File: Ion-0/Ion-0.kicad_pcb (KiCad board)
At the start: 4 copper layers, 54.6 x 86.4 mm, 96 parts, among them J1 Beaglebone-green-P9, J10 Conn_CAN, J11 Conn_Prob_1, J12 Conn_Prob_2, J13 Conn_01x04, J2 Beaglebone-green-P8, J3 Conn_02x06_Odd_Even, J4 Conn_02x06_Odd_Even, J5 Conn_02x06_Odd_Even, J6 Coaxial_Small, J8 Conn_Heater, J9 Conn_prob_3, Q1 IRLML6244, Q2 IRLML6244, U1 HDC2080, U2 MS5607-02BA, U3 BNO085, U4 TCA9617ADGKR, U6 MAX-M10M-00B, U7 TPS3850H50DRCR, U8 SN65HVD230, Y2 9HT10-32.768KBZF-T

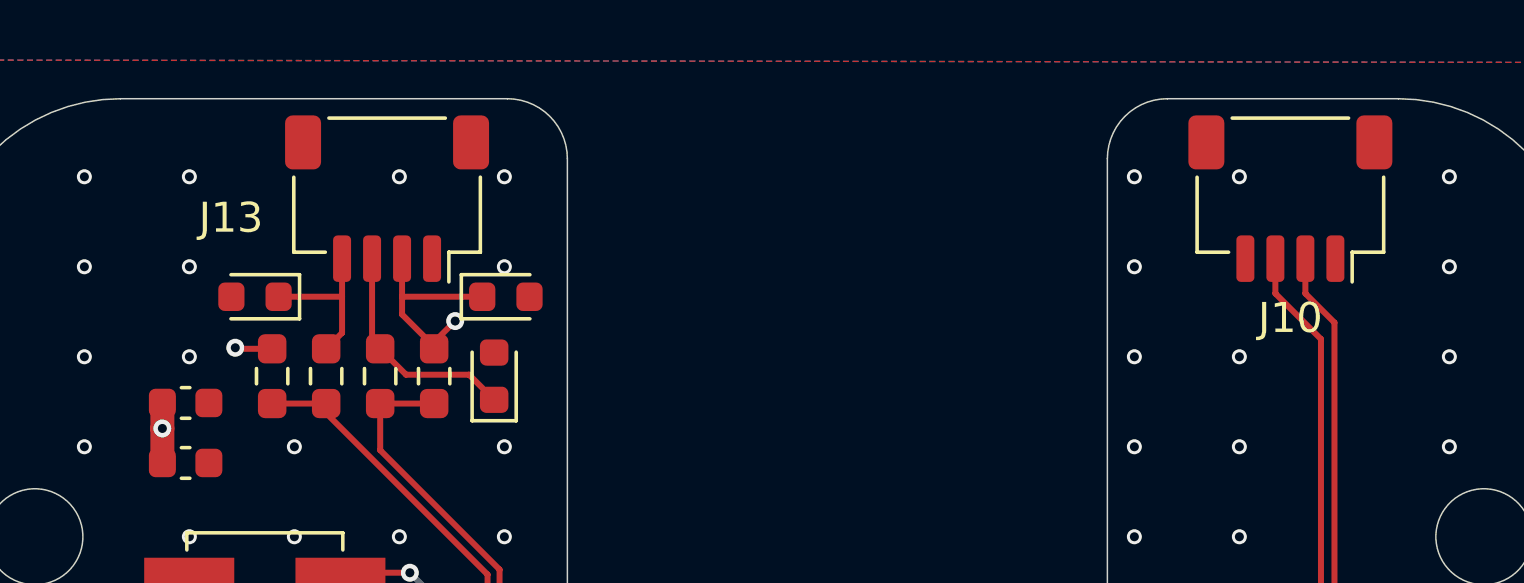
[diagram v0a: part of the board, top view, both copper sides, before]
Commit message: fixes in silkscreen
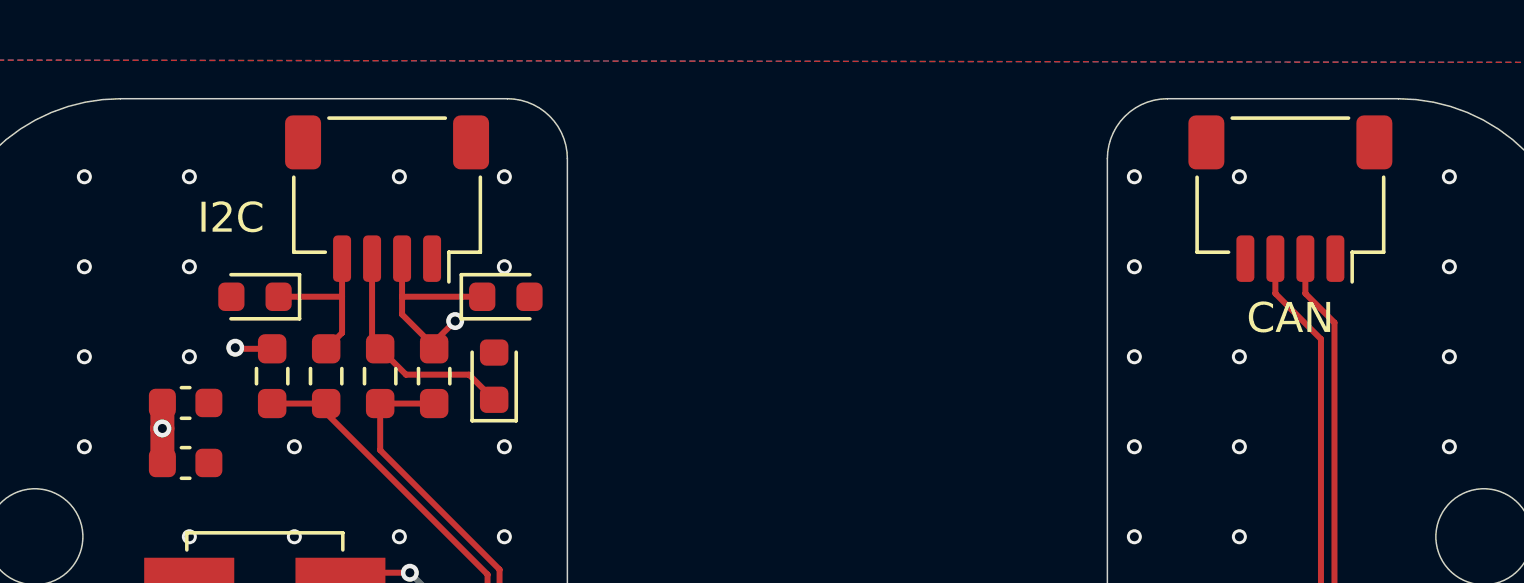
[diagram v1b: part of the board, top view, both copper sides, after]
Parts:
- renumbered J10 to CAN, J13 to I2C
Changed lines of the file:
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@@
 		(descr "JST SH series connector, SM04B-SRSS-TB (http://www.jst-mfg.com/product/pdf/eng/eSH.pdf)")
 		(tags "connector JST SH horizontal")
-		(property "Reference" "J13"
+		(property "Reference" "I2C"
 			(at 5.2025 -0.64 0)
 			(layer "F.SilkS")
@@
 		(descr "JST SH series connector, SM04B-SRSS-TB (http://www.jst-mfg.com/product/pdf/eng/eSH.pdf)")
 		(tags "connector JST SH horizontal")
-		(property "Reference" "J10"
+		(property "Reference" "CAN"
 			(at 0 -3.98 0)
 			(layer "F.SilkS")
@@
 		)
 	)
-	(group ""
-		(members "baa82daf-6091-4fa3-b979-6ad98ba0df5e")
-	)
 	(embedded_fonts no)

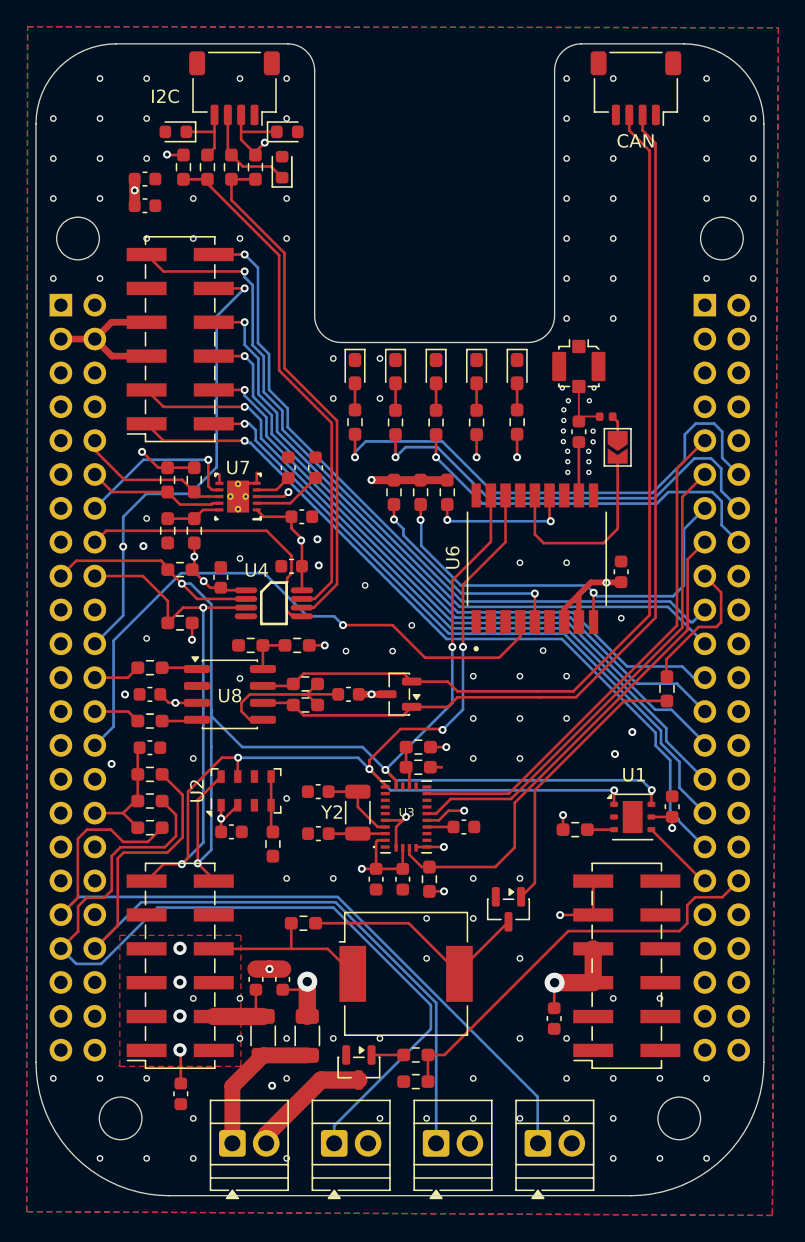
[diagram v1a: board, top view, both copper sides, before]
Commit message: allignment fix for power board
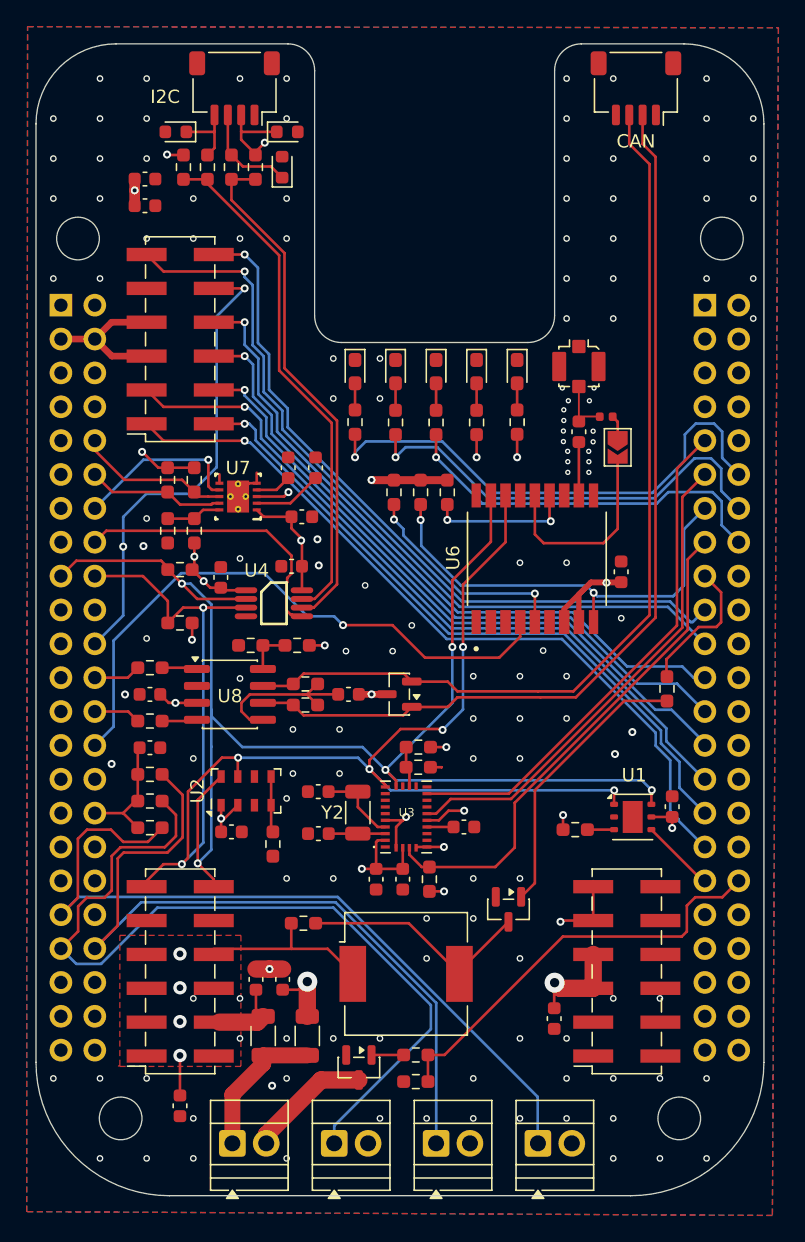
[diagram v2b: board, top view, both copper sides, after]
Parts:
- moved C17 0.90 mm to (132.0, 137.1)
- moved J3 0.42 mm to (165.5, 127.0)
- moved J4 0.42 mm to (132.0, 127.0)
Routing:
- net GND: vias 141 -> 145

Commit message: up to date
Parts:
- moved D2 1.43 mm to (157.3, 80.6)
- moved D3 1.43 mm to (154.2, 80.6)
- moved D4 1.43 mm to (151.2, 80.6)
- moved D5 1.43 mm to (148.2, 80.6)
- moved D6 1.43 mm to (145.1, 80.6)
- moved R30 1.43 mm to (157.3, 84.3)
- moved R31 1.43 mm to (154.2, 84.4)
- moved R32 1.43 mm to (151.2, 84.4)
- moved R33 1.43 mm to (148.2, 84.4)
- moved R34 1.43 mm to (145.1, 84.3)
- moved D8 0.17 mm to (139.9, 64.0)
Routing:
- net +5V: track 52.0 -> 53.5 mm
- net /GPIO_76: track 38.8 -> 39.4 mm
- net /GPIO_72: track 28.8 -> 29.4 mm
- net /GPIO_74: track 33.1 -> 33.7 mm
- net +3V3: vias 19 -> 20
- net GND: vias 145 -> 143
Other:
- outline, holes or cut-outs redrawn

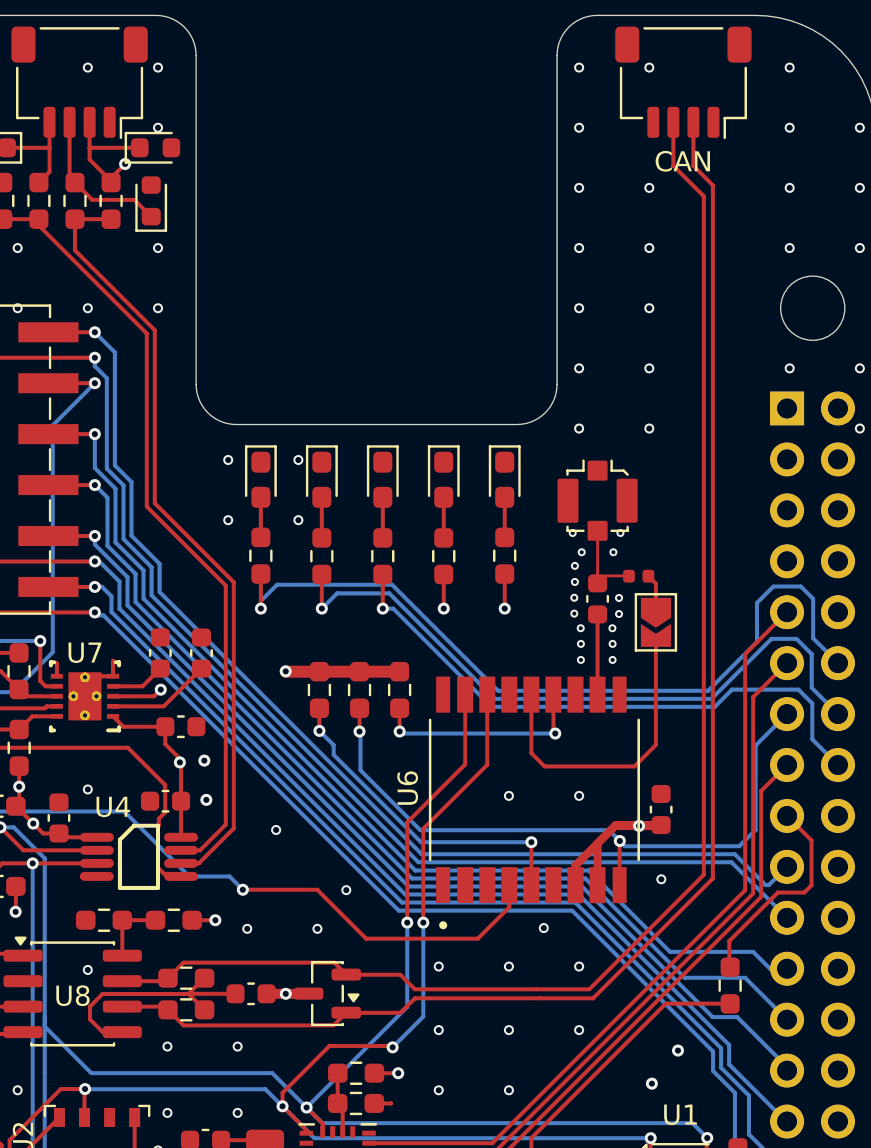
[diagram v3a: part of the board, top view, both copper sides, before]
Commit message: CAN trace fix
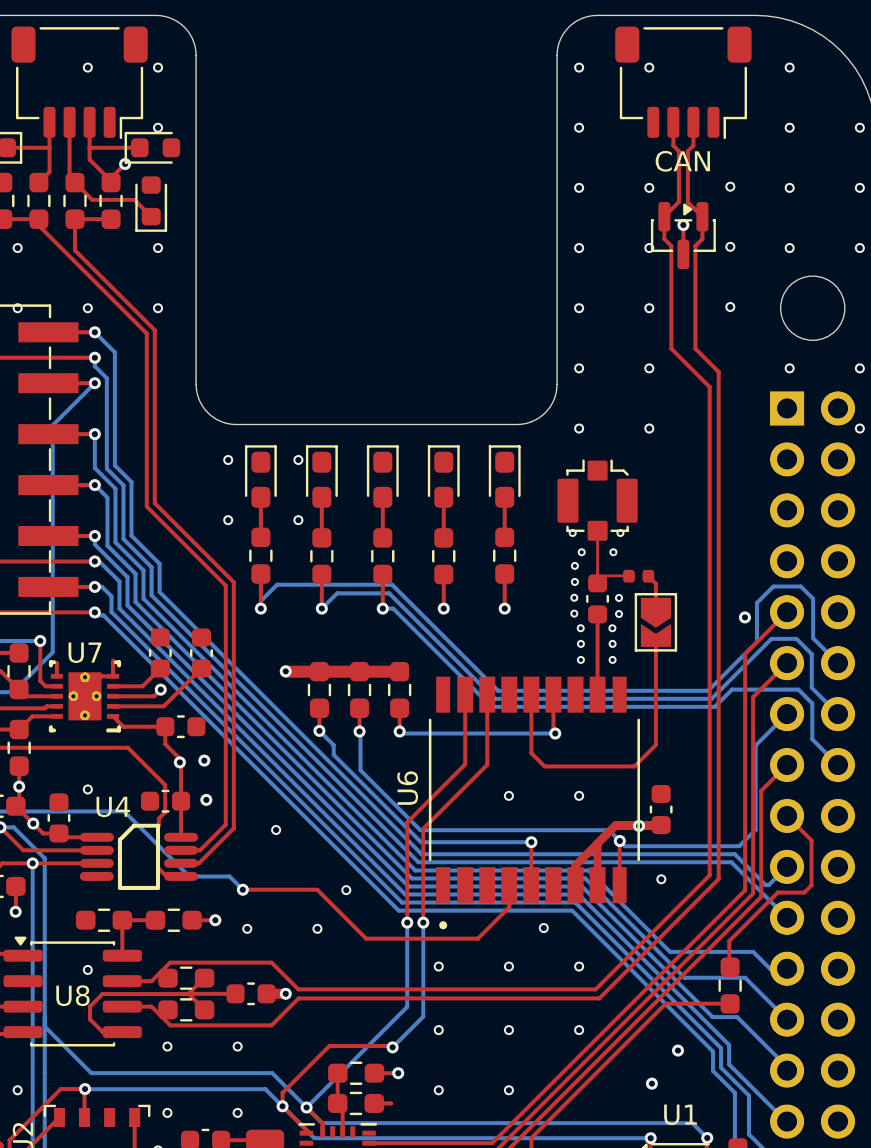
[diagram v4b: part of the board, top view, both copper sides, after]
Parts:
- moved D1 41.8 mm to (166.2, 68.4), turned to -90 degrees
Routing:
- net /Sensor-bus-hat/CAN_P: track 70.5 -> 71.5 mm
- net /Sensor-bus-hat/CAN_N: track 71.0 -> 71.9 mm
- net GND: track 19.6 -> 20.0 mm, vias 143 -> 148

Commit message: fixes in the schematic, made it better
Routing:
- net GND: vias 148 -> 146
- net +3V3: vias 20 -> 22
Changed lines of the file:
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@@
-	)
-	(via
-		(at 168.54 68.94)
-		(size 0.5)
-		(drill 0.3)
-		(layers "F.Cu" "B.Cu")
-		(net "GND")
 	)
 	(via
@@
 	)
 	(via
-		(at 168.54 71.94)
-		(size 0.5)
-		(drill 0.3)
-		(layers "F.Cu" "B.Cu")
-		(net "GND")
-	)
-	(via
 		(at 162.99 87.25)
 		(size 0.4)
@@
 	)
 	(via
+		(at 168.54 68.94)
+		(size 0.5)
+		(drill 0.3)
+		(layers "F.Cu" "B.Cu")
+		(net "+3V3")
+	)
+	(via
 		(at 142.86 102.52)
 		(size 0.6)
@@
 		(drill 0.3)
 		(layers "F.Cu" "B.Cu")
+		(net "+3V3")
+	)
+	(via
+		(at 168.54 71.94)
+		(size 0.5)
+		(drill 0.3)
+		(layers "F.Cu" "B.Cu")
